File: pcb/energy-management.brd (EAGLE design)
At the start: 113.3 x 53.7 mm, 83 parts, among them IC2 74LS595D, IC3 74LS595D, J1 WIRE_HOLE-14AWG, J2 WIRE_HOLE-14AWG, J3 WIRE_HOLE-14AWG, J4 WIRE_HOLE-14AWG, U1 DS1307

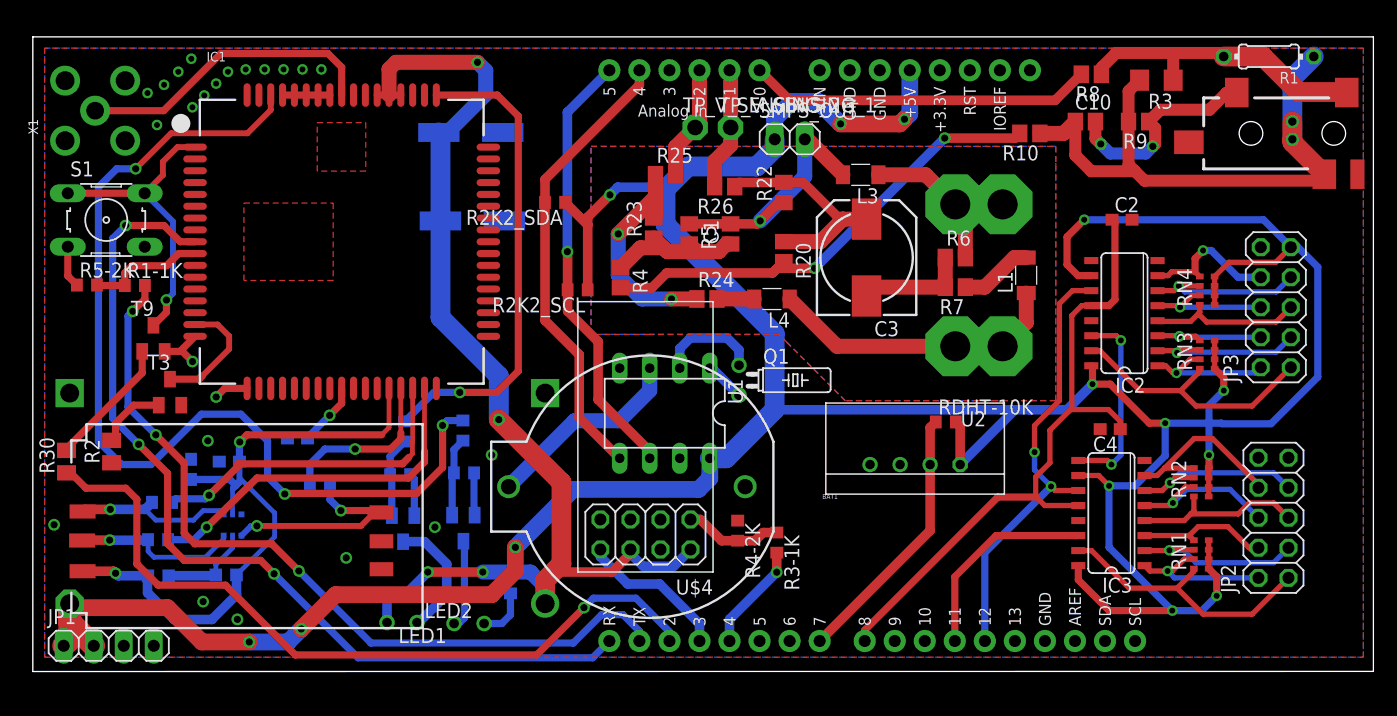
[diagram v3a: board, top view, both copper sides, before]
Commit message: put batt and reg on bottom, dht, ds, wifi on top
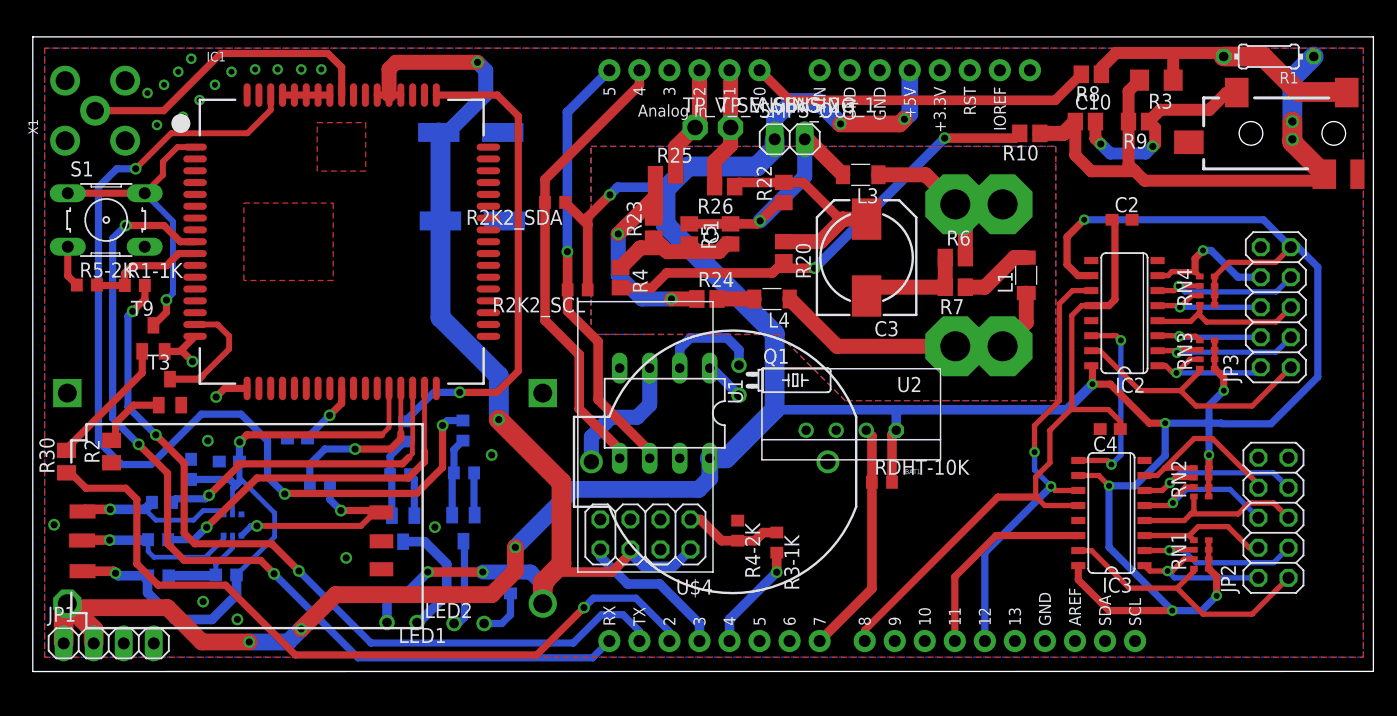
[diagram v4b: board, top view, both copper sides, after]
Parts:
- moved RDHT-10K 7.43 mm to (71.8, 16.0)
- moved BAT1 7.31 mm to (59.1, 17.7)
- moved U2 6.13 mm to (69.2, 20.4)
- moved U$2 0.20 mm to (1.22, 25.2)
- moved JP1 0.20 mm to (6.42, 2.38)
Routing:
- net N$23: track 17.2 -> 11.3 mm
- net VCC: track 315.5 -> 311.3 mm
- net DHT_DATA: track 22.6 -> 19.8 mm
- net GND: vias 25 -> 23
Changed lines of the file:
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@@
 <element name="CSIM_100N" library="rcl" package="C0603K" value="" x="16.35" y="8.17" rot="MR180"/>
 <element name="CSIM_22P" library="rcl" package="C0603K" value="" x="10.61" y="8.1" rot="MR0"/>
-<element name="U$2" library="bontor" package="DCDCMODULE" value="DCDCMODULE" x="1.42" y="25.24" rot="MR180"/>
+<element name="U$2" library="bontor" package="DCDCMODULE" value="DCDCMODULE" x="1.22" y="25.24" rot="MR180"/>
 <element name="IC1" library="microbuilder" package="SIM900_SMT" value="" x="26.12" y="36.34"/>
 <element name="R11-22" library="rcl" package="R0603" value="" x="24.28" y="15.92" rot="MR180"/>
@@
 </element>
 <element name="U1" library="adafruit" package="DIL08" value="DS1307" x="53.43" y="21.84" rot="R180"/>
-<element name="BAT1" library="SparkFun-Electromechanical" package="BATTCOM_20MM_PTH" value="" x="52.08" y="15.63" rot="R180"/>
+<element name="BAT1" library="SparkFun-Electromechanical" package="BATTCOM_20MM_PTH" value="" x="59.08" y="17.73" rot="R180"/>
 <element name="Q1" library="crystal" package="TC26H" value="" x="59.71" y="24.63" rot="R270">
 <attribute name="OC_NEWARK" value="unknown" x="59.71" y="24.63" size="1.778" layer="27" rot="R270" display="off"/>
@@
 <element name="R2K2_SCL" library="rcl" package="R0603" value="" x="46.07" y="32.27" rot="R180"/>
 <element name="R2K2_SDA" library="rcl" package="R0603" value="" x="44.16" y="39.67" rot="R180"/>
-<element name="JP1" library="pinhead" package="1X04" value="" x="6.42" y="2.18"/>
+<element name="JP1" library="pinhead" package="1X04" value="" x="6.42" y="2.38"/>
 <element name="U$4" library="tigorcustom" package="ESP8266" value="ESP8266" x="51.8" y="11.59" rot="R180"/>
 <element name="R3-1K" library="rcl" package="R0603" value="" x="62.91" y="10.9" rot="R270"/>
@@
 <element name="JP2" library="pinhead" package="2X05" value="" x="104.9" y="13" rot="R90"/>
 <element name="JP3" library="pinhead" package="2X05" value="" x="105.1" y="30.8" rot="R90"/>
-<element name="U2" library="RHT03_DHT-22_AM2302" package="RHT03_DHT-22" value="" x="74.6" y="17.5" rot="R180">
-<attribute name="PROD_ID" value="SEN-10167" x="74.6" y="17.5" size="1.778" layer="27" rot="R180" display="off"/>
+<element name="U2" library="RHT03_DHT-22_AM2302" package="RHT03_DHT-22" value="" x="69.2" y="20.4" rot="R180">
+<attribute name="PROD_ID" value="SEN-10167" x="69.2" y="20.4" size="1.778" layer="27" rot="R180" display="off"/>
 </element>
-<element name="RDHT-10K" library="rcl" package="R0603" value="" x="77.2" y="21.1"/>
+<element name="RDHT-10K" library="rcl" package="R0603" value="" x="71.8" y="16"/>
 </elements>
 <signals>
@@
 <via x="13.4" y="51.81" extent="1-16" drill="0.5"/>
 <via x="10.5" y="46.21" extent="1-16" drill="0.5"/>
-<via x="12.5" y="46.71" extent="1-16" drill="0.5"/>
-<via x="13.5" y="47.71" extent="1-16" drill="0.5"/>
-<via x="14.5" y="48.71" extent="1-16" drill="0.5"/>
-<via x="15.5" y="49.71" extent="1-16" drill="0.5"/>
-<via x="16.5" y="50.71" extent="1-16" drill="0.5"/>
-<via x="18" y="50.91" extent="1-16" drill="0.5"/>
-<via x="19.6" y="50.91" extent="1-16" drill="0.5"/>
-<via x="21.2" y="50.91" extent="1-16" drill="0.5"/>
-<via x="22.8" y="50.91" extent="1-16" drill="0.5"/>
+<via x="12.7" y="46.91" extent="1-16" drill="0.5"/>
+<via x="14.1" y="48.31" extent="1-16" drill="0.5"/>
+<via x="15.4" y="49.61" extent="1-16" drill="0.5"/>
+<via x="16.8" y="50.71" extent="1-16" drill="0.5"/>
+<via x="18.8" y="50.91" extent="1-16" drill="0.5"/>
+<via x="20.7" y="50.91" extent="1-16" drill="0.5"/>
+<via x="22.7" y="50.91" extent="1-16" drill="0.5"/>
 <via x="24.4" y="50.91" extent="1-16" drill="0.5"/>
 <contactref element="JP1" pad="3"/>
@@
 <wire x1="31.72" y1="6.73" x2="33.4" y2="8.41" width="0.8128" layer="16"/>
 <wire x1="33.4" y1="8.41" x2="38.05" y2="8.41" width="0.8128" layer="1"/>
-<wire x1="43.32" y1="5.74" x2="43.32" y2="7.18" width="1.27" layer="16"/>
-<wire x1="43.32" y1="7.18" x2="42.09" y2="8.41" width="1.27" layer="16"/>
 <wire x1="42.09" y1="8.41" x2="38.05" y2="8.41" width="1.27" layer="16"/>
 <wire x1="50.53" y1="9.97" x2="51.6" y2="8.9" width="0.8128" layer="16"/>
@@
 <wire x1="39.4" y1="21.3" x2="44.7" y2="16" width="1.6764" layer="1"/>
 <wire x1="44.7" y1="16" x2="44.7" y2="9.1" width="1.6764" layer="1"/>
-<wire x1="44.7" y1="9.1" x2="43.32" y2="7.72" width="1.6764" layer="1"/>
-<wire x1="43.32" y1="7.72" x2="43.32" y2="7.6" width="1.6764" layer="1"/>
-<wire x1="43.32" y1="7.6" x2="43.32" y2="5.74" width="1.6764" layer="1"/>
+<wire x1="44.7" y1="9.1" x2="43.25" y2="7.65" width="1.6764" layer="1"/>
+<wire x1="43.25" y1="7.65" x2="43.12" y2="7.52" width="1.6764" layer="1"/>
 <wire x1="48.97" y1="8.41" x2="44.13" y2="8.41" width="0.8128" layer="1"/>
 <wire x1="44.13" y1="8.41" x2="43.32" y2="7.6" width="0.8128" layer="1"/>
+<wire x1="42.09" y1="8.41" x2="43.12" y2="7.38" width="1.27" layer="16"/>
+<wire x1="43.12" y1="7.38" x2="43.12" y2="5.74" width="1.27" layer="16"/>
+<wire x1="43.12" y1="7.52" x2="43.12" y2="5.74" width="1.6764" layer="1"/>
+<wire x1="43.32" y1="7.6" x2="43.27" y2="7.65" width="1.6764" layer="1"/>
+<wire x1="43.27" y1="7.65" x2="43.25" y2="7.65" width="1.6764" layer="1"/>
 </signal>
 <signal name="USIM_CLK">
@@
 <wire x1="68.3" y1="46.3" x2="66.4" y2="48.2" width="1.4224" layer="16"/>
 <wire x1="66.4" y1="48.2" x2="64.2" y2="48.2" width="1.4224" layer="16"/>
-<wire x1="3.12" y1="5.74" x2="3.12" y2="4.21" width="1.9304" layer="1"/>
-<wire x1="3.12" y1="4.21" x2="5.15" y2="2.18" width="1.9304" layer="1"/>
-<wire x1="2.61" y1="2.18" x2="3.12" y2="2.69" width="1.9304" layer="1"/>
-<wire x1="3.12" y1="2.69" x2="3.12" y2="5.74" width="1.9304" layer="1"/>
-<wire x1="3.12" y1="5.74" x2="3.46" y2="5.4" width="1.4224" layer="1"/>
+<wire x1="2.92" y1="5.74" x2="3.46" y2="5.4" width="1.4224" layer="1"/>
 <wire x1="3.46" y1="5.4" x2="11.4" y2="5.4" width="1.4224" layer="1"/>
 <wire x1="11.4" y1="5.4" x2="14.3" y2="2.5" width="1.4224" layer="1"/>
@@
 <via x="89.6" y="24.3" extent="1-16" drill="0.5"/>
 <wire x1="89.6" y1="24.3" x2="87.43" y2="22.13" width="0.8128" layer="16"/>
-<wire x1="87.43" y1="22.13" x2="84.3" y2="22.13" width="0.8128" layer="16"/>
-<wire x1="83.04" y1="22.13" x2="62.73" y2="22.13" width="0.8128" layer="16"/>
+<wire x1="87.43" y1="22.13" x2="72.9" y2="22.13" width="0.8128" layer="16"/>
+<wire x1="72.9" y1="22.13" x2="62.73" y2="22.13" width="0.8128" layer="16"/>
 <wire x1="95.75" y1="21" x2="94.4" y2="21" width="0.6096" layer="1"/>
 <wire x1="94.4" y1="21" x2="91.1" y2="24.3" width="0.6096" layer="1"/>
@@
 <contactref element="U2" pad="VDD"/>
 <contactref element="RDHT-10K" pad="2"/>
-<wire x1="78.05" y1="21.1" x2="78.41" y2="20.74" width="0.8128" layer="1"/>
-<wire x1="78.41" y1="20.74" x2="78.41" y2="17.5" width="0.8128" layer="1"/>
-<wire x1="78.41" y1="17.5" x2="83.04" y2="22.13" width="0.8128" layer="16"/>
-<wire x1="83.04" y1="22.13" x2="84.3" y2="22.13" width="0.8128" layer="16"/>
+<wire x1="72.65" y1="16" x2="72.65" y2="20.04" width="0.8128" layer="1"/>
+<wire x1="73.01" y1="20.4" x2="73.01" y2="22.02" width="0.8128" layer="16"/>
+<wire x1="73.01" y1="22.02" x2="72.9" y2="22.13" width="0.8128" layer="16"/>
+<wire x1="73.01" y1="20.4" x2="72.65" y2="20.04" width="0.8128" layer="1"/>
+<wire x1="2.92" y1="5.74" x2="2.61" y2="5.43" width="1.6764" layer="1"/>
+<wire x1="2.61" y1="5.43" x2="2.61" y2="2.38" width="1.6764" layer="1"/>
+<wire x1="5.15" y1="2.38" x2="5.15" y2="3.51" width="1.6764" layer="1"/>
+<wire x1="5.15" y1="3.51" x2="2.92" y2="5.74" width="1.6764" layer="1"/>
 </signal>
 <signal name="SCL">
@@
 <contactref element="R2K2_SDA" pad="2"/>
 <contactref element="U$1" pad="A4"/>
-<wire x1="49.62" y1="18.03" x2="46.2" y2="21.45" width="0.8128" layer="1"/>
-<wire x1="46.2" y1="21.45" x2="46.2" y2="26.8" width="0.8128" layer="1"/>
 <wire x1="46.2" y1="26.8" x2="43.31" y2="29.69" width="0.8128" layer="1"/>
 <wire x1="43.31" y1="29.69" x2="43.31" y2="39.67" width="0.8128" layer="1"/>
@@
 <wire x1="43.31" y1="41.61" x2="51.29" y2="49.59" width="0.8128" layer="1"/>
 <wire x1="51.29" y1="49.59" x2="51.29" y2="50.84" width="0.8128" layer="1"/>
+<wire x1="46.2" y1="26.8" x2="46.2" y2="22.2" width="0.8128" layer="1"/>
+<wire x1="46.2" y1="22.2" x2="49.62" y2="18.78" width="0.8128" layer="1"/>
+<wire x1="49.62" y1="18.78" x2="49.62" y2="18.03" width="0.8128" layer="1"/>
 </signal>
 <signal name="N$23">
 <contactref element="U1" pad="3"/>
 <contactref element="BAT1" pad="1"/>
-<wire x1="40.23" y1="15.63" x2="45.8" y2="21.2" width="1.27" layer="16"/>
-<wire x1="45.8" y1="21.2" x2="49.6" y2="21.2" width="1.27" layer="16"/>
-<wire x1="49.6" y1="21.2" x2="52.16" y2="23.76" width="1.27" layer="16"/>
-<wire x1="52.16" y1="23.76" x2="52.16" y2="25.65" width="1.27" layer="16"/>
+<wire x1="52.16" y1="22.56" x2="52.16" y2="25.65" width="1.27" layer="16"/>
+<wire x1="47.23" y1="17.73" x2="47.23" y2="19.83" width="1.27" layer="16"/>
+<wire x1="47.23" y1="19.83" x2="48.9" y2="21.5" width="1.27" layer="16"/>
+<wire x1="48.9" y1="21.5" x2="51.1" y2="21.5" width="1.27" layer="16"/>
+<wire x1="51.1" y1="21.5" x2="52.16" y2="22.56" width="1.27" layer="16"/>
 </signal>
 <signal name="VIN">
@@
 <contactref element="RDHT-10K" pad="1"/>
 <contactref element="U$1" pad="D7"/>
-<wire x1="76.35" y1="21.1" x2="75.87" y2="20.62" width="0.8128" layer="1"/>
-<wire x1="75.87" y1="20.62" x2="75.87" y2="17.5" width="0.8128" layer="1"/>
-<wire x1="75.87" y1="17.5" x2="75.87" y2="11.92" width="0.8128" layer="1"/>
-<wire x1="75.87" y1="11.92" x2="66.53" y2="2.58" width="0.8128" layer="1"/>
+<wire x1="70.95" y1="16" x2="70.95" y2="19.92" width="0.8128" layer="1"/>
+<wire x1="70.95" y1="19.92" x2="70.47" y2="20.4" width="0.8128" layer="1"/>
+<wire x1="66.53" y1="2.58" x2="70.95" y2="7" width="0.8128" layer="1"/>
+<wire x1="70.95" y1="7" x2="70.95" y2="16" width="0.8128" layer="1"/>
 </signal>
 <signal name="N$32">
@@
 </signal>
 </signals>
+<errors>
+</errors>
 </board>
 </drawing>

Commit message: remove resistor and cutout on analog line
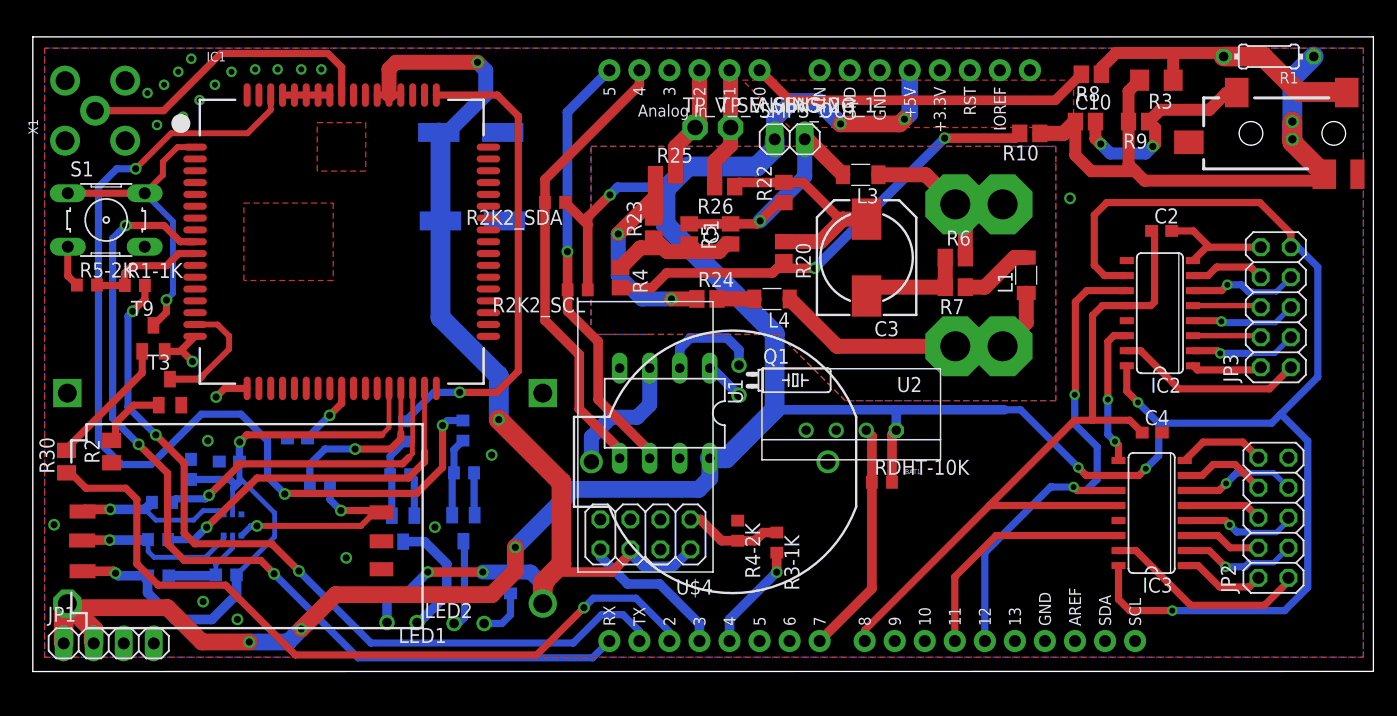
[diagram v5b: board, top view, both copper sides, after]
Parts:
- removed RN1, RN2, RN3, RN4: (no value), resistor-dil:0603-ARC
- moved C4 3.56 mm to (94.7, 20.2), turned to 0 degrees
- moved C2 3.48 mm to (95.5, 37.2)
- moved IC3 3.40 mm to (94.6, 13.4)
- moved IC2 3.00 mm to (95.3, 30.3)
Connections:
- net OUT_1: no longer RN1.4
- net OUT_10: no longer RN3.3
- net OUT_11: no longer RN3.2
- net OUT_12: no longer RN3.1
- net OUT_13: no longer RN4.4
- net OUT_14: no longer RN4.3
- net OUT_15: no longer RN4.2
- net OUT_16: no longer RN4.1
- net OUT_2: no longer RN1.3
- net OUT_3: no longer RN1.2
- net OUT_4: no longer RN1.1
- net OUT_5: no longer RN2.4
- net OUT_6: no longer RN2.3
- net OUT_7: no longer RN2.2
- net OUT_8: no longer RN2.1
- net OUT_9: no longer RN3.4
- net VCC: no longer RN1.5, RN1.6, RN1.7, RN1.8, RN2.5, RN2.6, RN2.7, RN2.8, RN3.5, RN3.6, RN3.7, RN3.8, RN4.5, RN4.6, RN4.7, RN4.8
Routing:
- net VCC: track 311.3 -> 288.5 mm, vias 14 -> 10
- net GND: track 51.8 -> 69.2 mm, vias 23 -> 24
- net OUT_8: track 15.3 -> 7.43 mm
- net OUT_6: track 13.7 -> 6.66 mm, vias 1 -> 0
- net ST_CP: track 56.9 -> 63.8 mm
- net OUT_9: track 22.7 -> 16.0 mm
- net SH_CP: track 37.9 -> 44.3 mm
- net OUT_1: track 23.5 -> 17.4 mm
- net OUT_10: track 11.6 -> 5.97 mm, vias 1 -> 0
- net OUT_7: track 15.5 -> 9.91 mm
- net OUT_2: track 12.7 -> 7.30 mm, vias 1 -> 0
- net OUT_16: track 11.8 -> 6.39 mm, vias 1 -> 0
- net OUT_3: track 15.2 -> 10.0 mm
- net OUT_14: track 10.9 -> 5.79 mm, vias 1 -> 0
- net OUT_5: track 14.9 -> 9.84 mm, vias 0 -> 1
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- added copper zone on layer 1, net N$31
